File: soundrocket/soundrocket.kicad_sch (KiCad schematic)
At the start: 11 parts, among them J1 XLR3 MALE (OUT), SW1 SW_Push, SW2 RotaryEncoder_Switch, T1 PE-65612NL, U1 Teensy4.0, U2 DIT4192IPW, U3 TPS63061

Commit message: Hardware Test & Revision 2
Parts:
- removed U3: TPS63061, Package_SON:Texas_S-PWSON-N10_ThermalVias, symbol Regulator_Switching:TPS63061
- added R1, R2, R3, R4: R_Small (10k), KiCad Models:STA_CF14_STP, symbol Device:R_Small_US
- added R5: R_Small, KiCad Models:STA_CF14_STP, symbol Device:R_Small_US
- J1: footprint Connector_Audio:Jack_XLR_Neutrik_NC3FAAH-0_Horizontal -> Connector_Audio:Jack_XLR_Neutrik_NC3MAAV_Vertical
- renumbered C3 to C1, C4 to C2, C1 to C3, C2 to C4
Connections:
- net GND: now also SW1.1, SW2.S1
- net at C1.1: now also SW1.2, U1.4 (2_OUT2), R5.1; no longer SW1.1
- net at C2.1: now also SW2.S2, U1.5 (3_LRCLK2); no longer SW2.S1
- net at C4.1, U1.7 (5_IN2): now also R3.1; no longer SW2.B
- net at C3.1, U1.8 (6_OUT1D): now also R4.1; no longer SW2.A
- net 3V3: now reaches U1.31 (3V3), U2.7 (V_IO)
- net 3V3: now also R1.2, R2.2, R5.2
- new net: R2.1, R3.2, SW2.B
- new net: R1.1, R4.2, SW2.A
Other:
- moved on the sheet: C1, C2, C3, C4, SW1, SW2, U1

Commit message: Prototype Revision 2
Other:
- moved on the sheet: C1, C2, C3, C4, J1, R1, R2, R3, R4, R5, SW1, SW2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

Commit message: Shrink
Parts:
- removed J1: XLR3 MALE (OUT), Connector_Audio:Jack_XLR_Neutrik_NC3MAAV_Vertical, symbol Connector_Audio:XLR3
- removed U1: Teensy4.0, KiCad Models:Teensy40, symbol teensy:Teensy4.0
- added H1: XLR-, symbol Mechanical:MountingHole_Pad_MP
- added H2: XLR+, symbol Mechanical:MountingHole_Pad_MP
- added H3: GND, symbol Mechanical:MountingHole_Pad_MP
- added U3: STM32U545CETxQ, KiCad Models:STM32U545CET6Q, symbol MCU_ST_STM32U5:STM32U545CETxQ
- C2, C3, C4, R1, R2, R3, R4, SW2: now not fitted; now left out of the parts list
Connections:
- net GND: now also H3.MP
- net XLR-TX+: now also H2.MP
- net XLR-TX-: now also H1.MP
- new net: U3.24 (VSS), U3.35 (VSS), U3.47 (VSS)

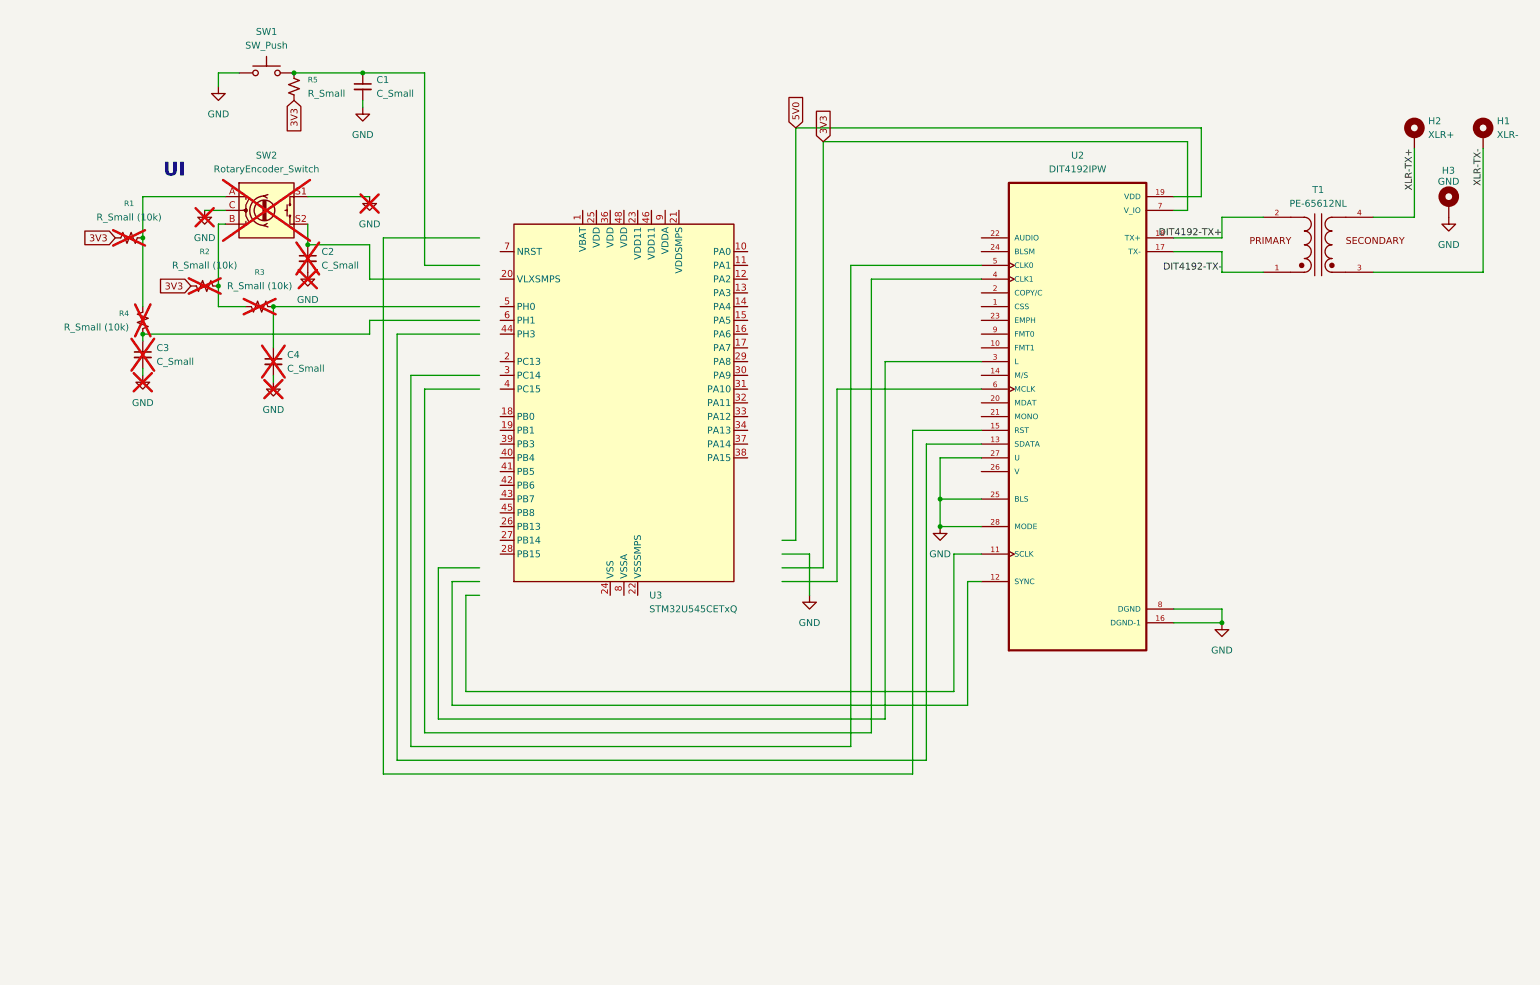
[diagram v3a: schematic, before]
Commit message: stm32 running out of space
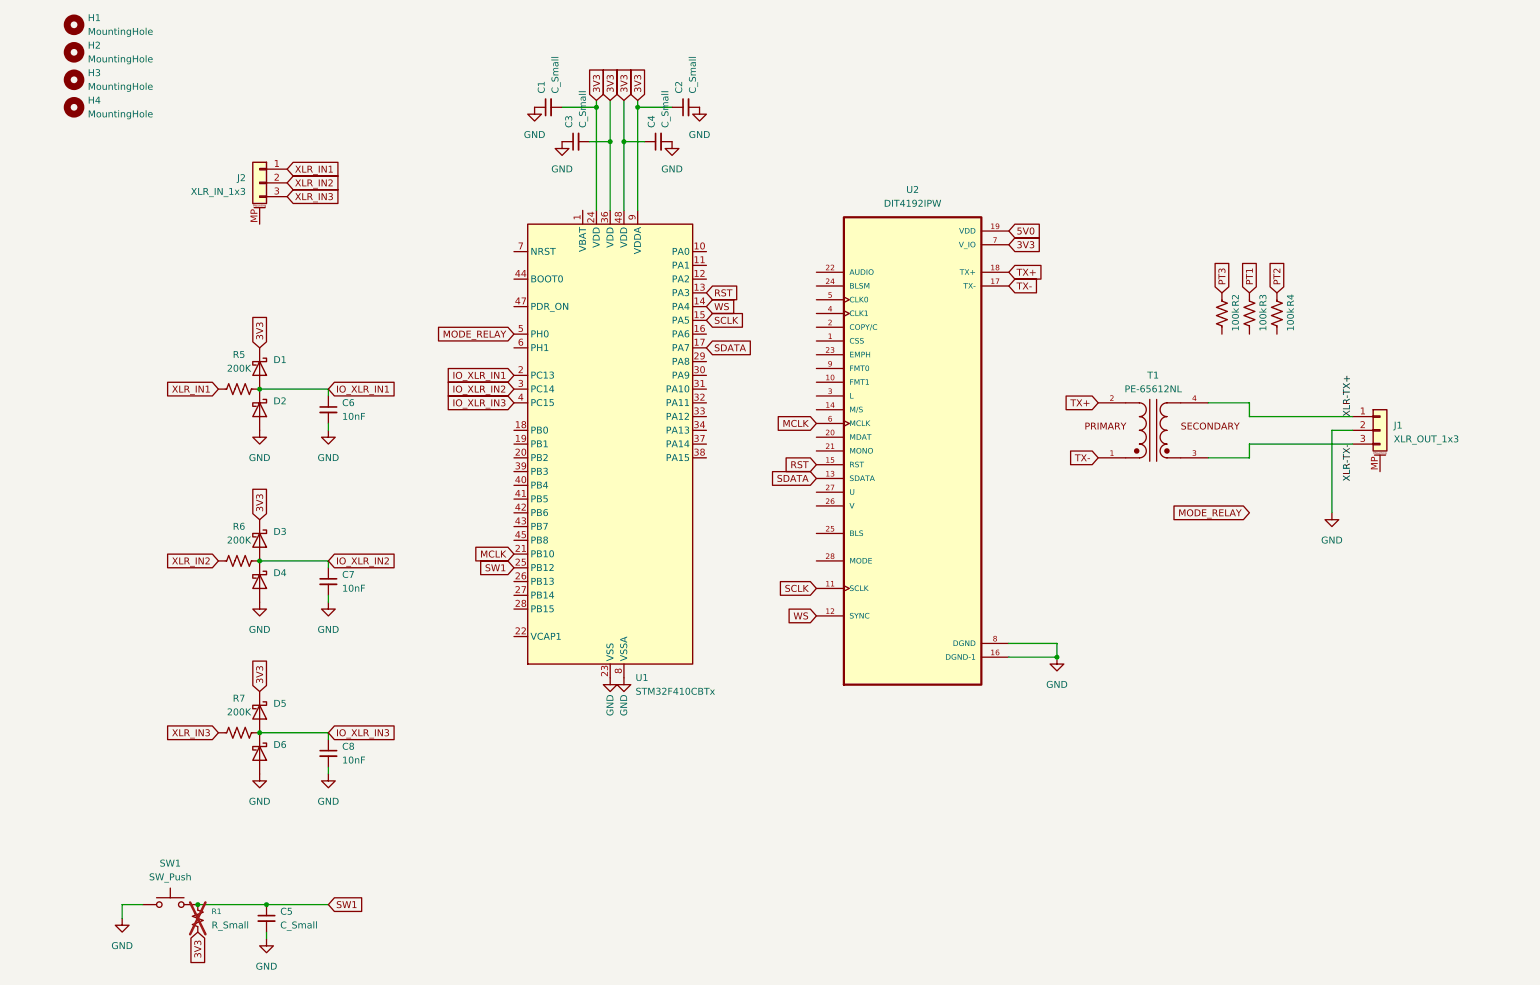
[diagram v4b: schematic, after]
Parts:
- removed H1: XLR-, symbol Mechanical:MountingHole_Pad_MP
- removed H2: XLR+, symbol Mechanical:MountingHole_Pad_MP
- removed H3: GND, symbol Mechanical:MountingHole_Pad_MP
- removed R1, R2, R3, R4: R_Small (10k), KiCad Models:STA_CF14_STP, symbol Device:R_Small_US
- removed SW2: RotaryEncoder_Switch, Rotary_Encoder:RotaryEncoder_Bourns_Vertical_PEC12R-3x17F-Sxxxx, symbol Device:RotaryEncoder_Switch
- removed U3: STM32U545CETxQ, KiCad Models:STM32U545CET6Q, symbol MCU_ST_STM32U5:STM32U545CETxQ
- added C1: C_Small, Capacitor_SMD:C_0402_1005Metric, symbol Device:C_Small
- added C6, C7, C8: 10nF, Capacitor_SMD:C_0402_1005Metric, symbol Device:C_Small
- added D1, D2, D3, D4, D5, D6: Schottky, Diode_SMD:D_SOD-323, symbol Device:D_Schottky
- added H1, H2, H3, H4: MountingHole, MountingHole:MountingHole_2.2mm_M2, symbol Mechanical:MountingHole
- added J1: XLR_OUT_1x3, Connector_PinHeader_1.00mm:PinHeader_1x03_P1.00mm_Vertical, symbol Connector_Generic_MountingPin:Conn_01x03_MountingPin
- added J2: XLR_IN_1x3, Connector_PinHeader_1.00mm:PinHeader_1x03_P1.00mm_Vertical, symbol Connector_Generic_MountingPin:Conn_01x03_MountingPin
- added R2, R3, R4: 100k, Resistor_SMD:R_0402_1005Metric, symbol Device:R_US
- added R5, R6, R7: 200K, Resistor_SMD:R_0402_1005Metric, symbol Device:R_US
- added U1: STM32F410CBTx, Package_QFP:LQFP-48_7x7mm_P0.5mm, symbol MCU_ST_STM32F4:STM32F410CBTx
- C2, C3, C4: footprint KiCad Models:CAPRR254W54L381T254H466 -> Capacitor_SMD:C_0402_1005Metric; now fitted; now in the parts list
- R1: renamed from R5; now not fitted
- SW1: footprint Button_Switch_THT:SW_PUSH-12mm -> KiCad Models:SW_D6_C_90
- renumbered C1 to C5
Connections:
- net 3V3: now also C2.1, C3.2, C4.1, C1.2, D1.1 (K), D3.1 (K), D5.1 (K), U1.24 (VDD), U1.36 (VDD), U1.48 (VDD), U1.9 (VDDA)
- net GND: now also C3.1, C1.1, C6.2, C7.2, C8.2, D2.2 (A), D4.2 (A), D6.2 (A), J1.2 (Pin_2), U1.23 (VSS), U1.35 (VSS), U1.46 (VSS), U1.8 (VSSA); no longer C3.2, U2.25 (BLS), U2.27 (U), U2.28 (MODE)
- net XLR-TX+: now also J1.1 (Pin_1)
- net XLR-TX-: now also J1.3 (Pin_3)
- net SW1: now reaches C5.1, R1.1, SW1.2
- net SW1: now also U1.25 (PB12)
- net SCLK: now reaches U2.11 (SCLK)
- net SCLK: now also U1.15 (PA5)
- net WS: now reaches U2.12 (SYNC)
- net WS: now also U1.14 (PA4)
- net SDATA: now reaches U2.13 (SDATA)
- net SDATA: now also U1.17 (PA7)
- net RST: now reaches U2.15 (RST)
- net RST: now also U1.13 (PA3)
- net MCLK: now reaches U2.6 (MCLK)
- net MCLK: now also U1.21 (PB10)
- net DIT4192-TX+ renamed TX+
- net DIT4192-TX- renamed TX-
- new net IO_XLR_IN1: C6.1, D1.2 (A), D2.1 (K), R5.2, U1.2 (PC13)
- new net IO_XLR_IN2: C7.1, D3.2 (A), D4.1 (K), R6.2, U1.3 (PC14)
- new net IO_XLR_IN3: C8.1, D5.2 (A), D6.1 (K), R7.2, U1.4 (PC15)
- new net MODE_RELAY: U1.5 (PH0)
- new net PT1: R3.1
- new net PT2: R4.1
- new net PT3: R2.1
- new net XLR_IN1: J2.1 (Pin_1), R5.1
- new net XLR_IN2: J2.2 (Pin_2), R6.1
- new net XLR_IN3: J2.3 (Pin_3), R7.1
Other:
- note removed: "UI"
- moved on the sheet: C5, SW1, T1, U2
